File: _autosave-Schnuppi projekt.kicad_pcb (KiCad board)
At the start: 2 copper layers, 23 parts, among them Q1 BC817, Q2 BC817, SW1 SW_Push, SW2 SW_Push, SW3 SW_Push, SW4 SW_Push, SW5 SW_Push, SW6 SW_Push, U13 ESP32-WROOM-32E, U14 DM-OLED096-636, U2 TPS62065DSGR, U5 WE-TVS-82400102, U6 CH340C

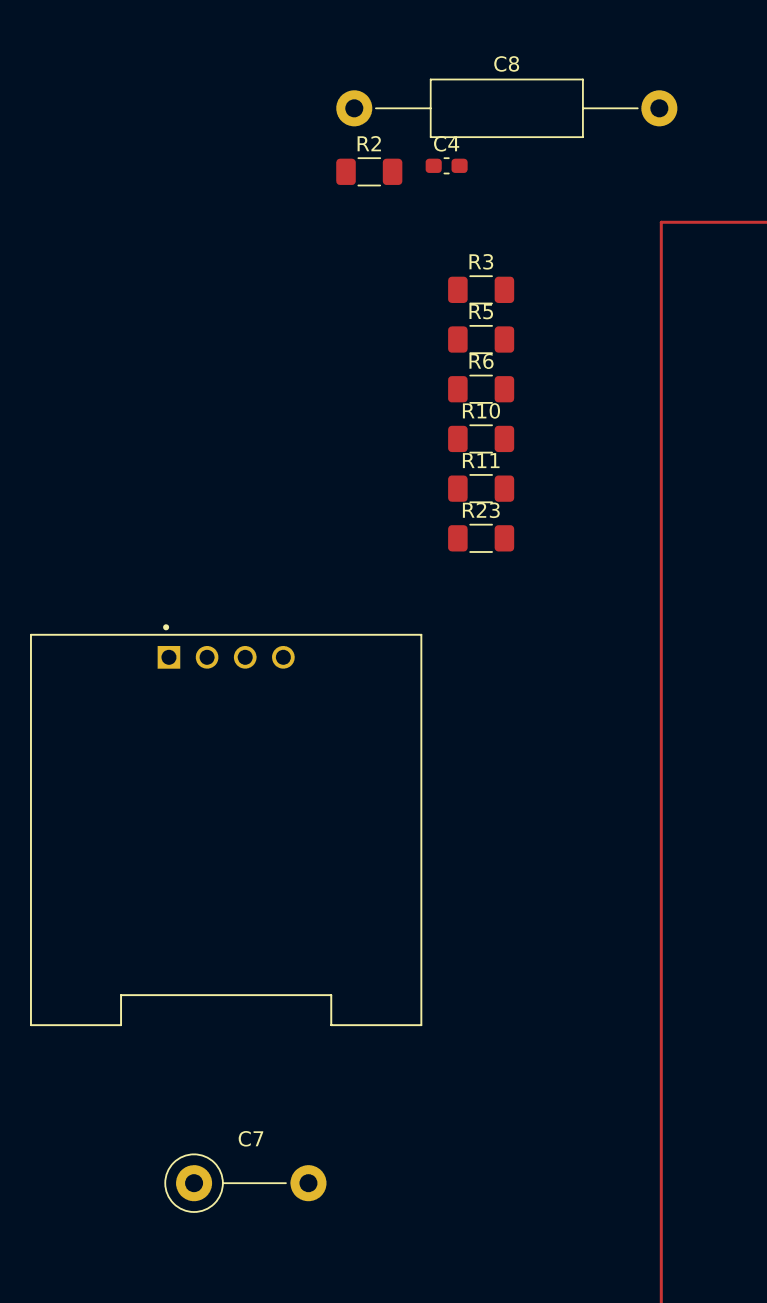
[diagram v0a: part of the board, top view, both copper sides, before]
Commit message: changed resistors
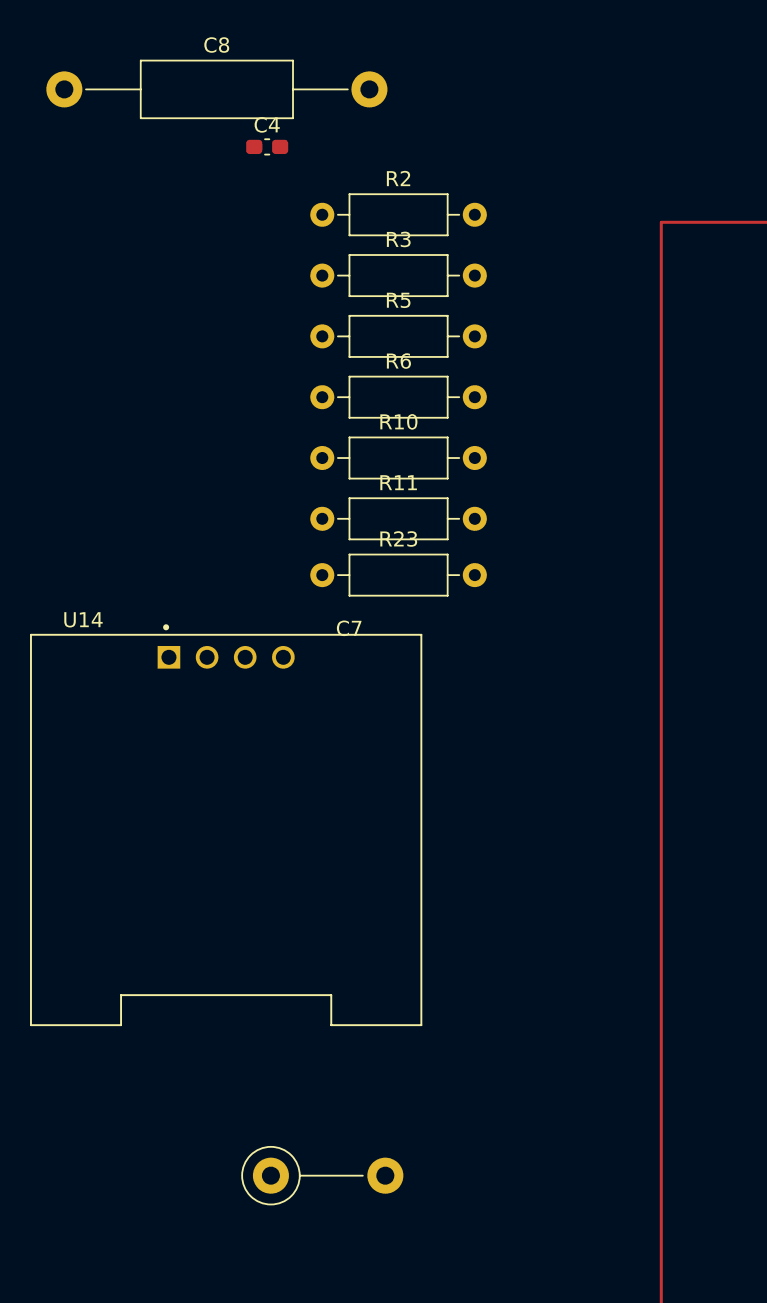
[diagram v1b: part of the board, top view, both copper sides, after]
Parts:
- R10, R11, R2, R23, R3, R5, R6: footprint Resistor_SMD:R_1206_3216Metric_Pad1.30x1.75mm_HandSolder -> Resistor_THT:R_Axial_DIN0207_L6.3mm_D2.5mm_P10.16mm_Horizontal
- moved C8 19.4 mm to (-29.8, 1.15)
- moved C4 12.0 mm to (-16.2, 4.98)
- moved R23 10.9 mm to (-12.6, 33.5)
- moved R11 10.8 mm to (-12.6, 29.8)
- moved R10 10.7 mm to (-12.6, 25.7)
- moved R3 10.6 mm to (-12.6, 13.6)
- moved R6 10.6 mm to (-12.6, 21.6)
- moved R5 10.6 mm to (-12.6, 17.6)
- moved C7 5.14 mm to (-16.0, 73.5)
- moved R2 4.24 mm to (-12.6, 9.50)

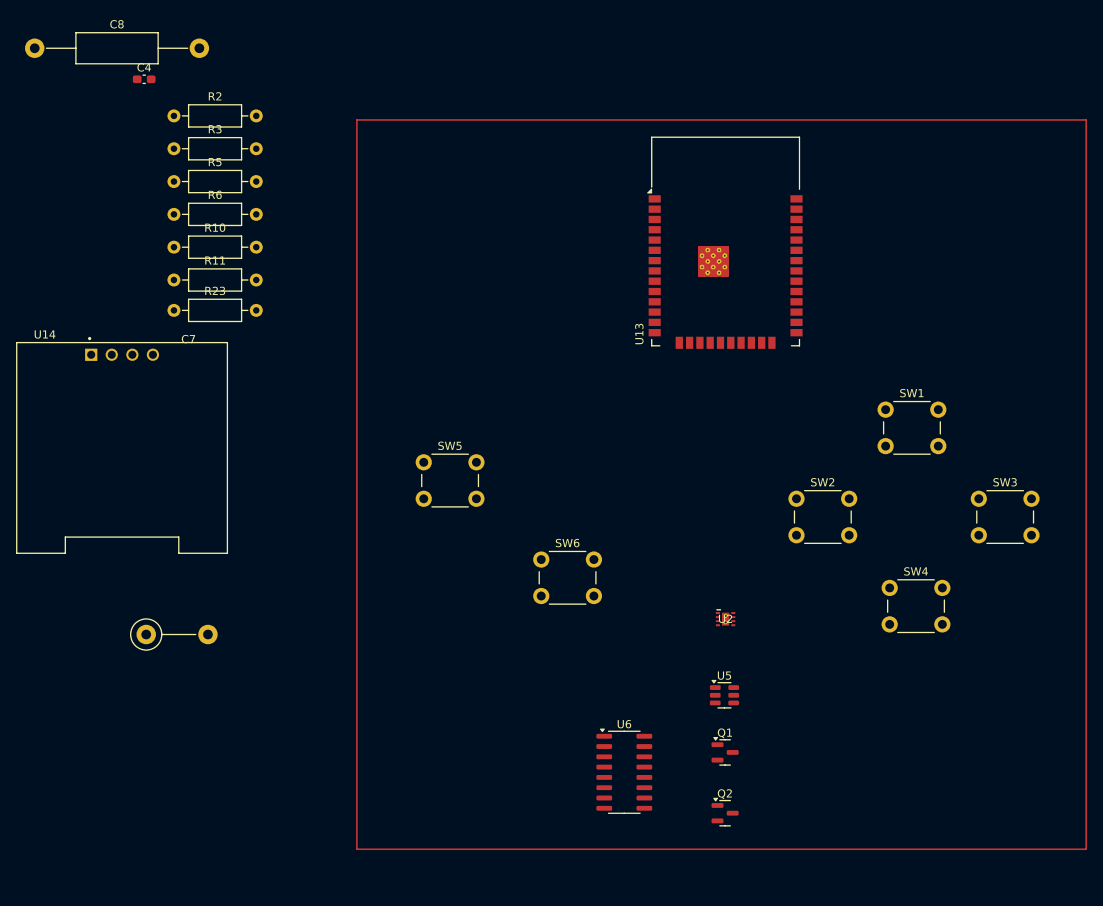
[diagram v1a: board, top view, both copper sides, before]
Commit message: added footprints for resistors
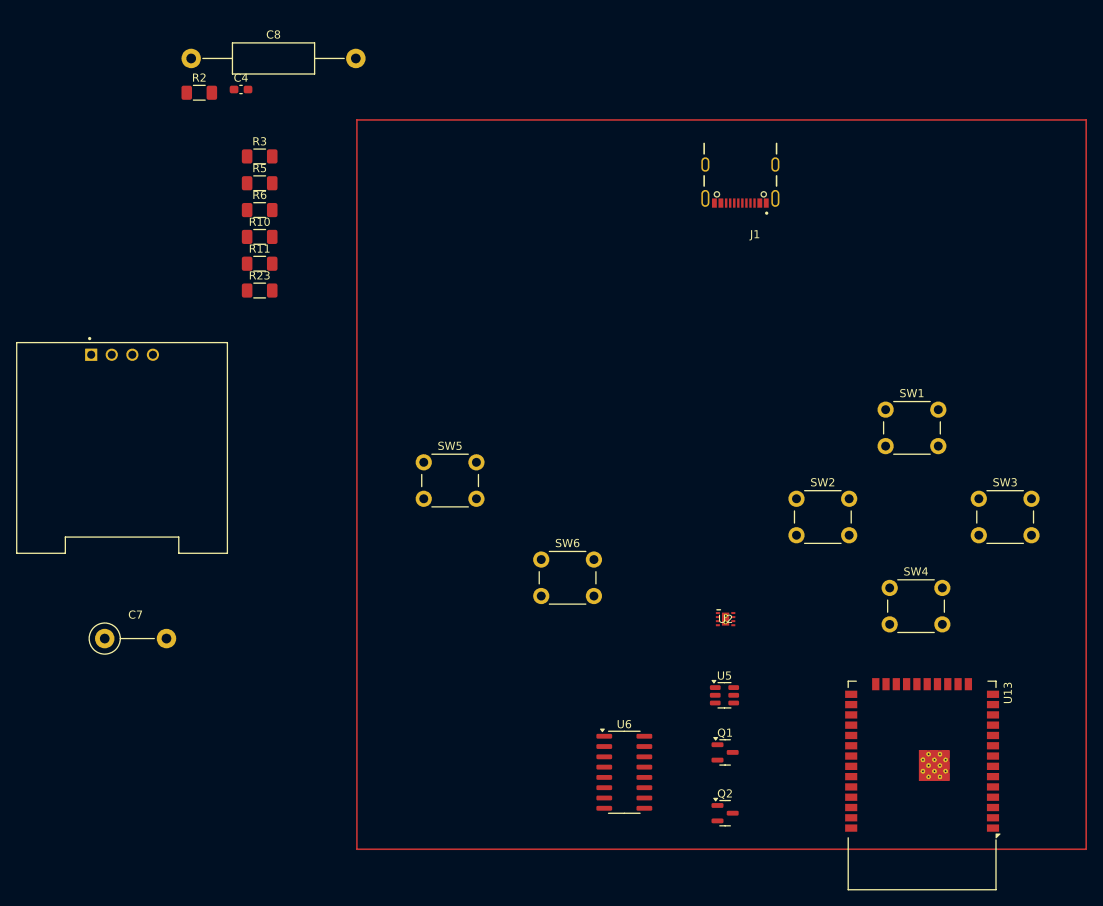
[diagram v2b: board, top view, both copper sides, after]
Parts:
- added J1: USB4105-GF-A, USB4105-GF-A (2):GCT_USB4105-GF-A, F.Cu at (57.3, 15.5)
- R10, R11, R2, R23, R3, R5, R6: footprint Resistor_THT:R_Axial_DIN0207_L6.3mm_D2.5mm_P10.16mm_Horizontal -> Resistor_SMD:R_1206_3216Metric_Pad1.30x1.75mm_HandSolder
- moved U13 65.8 mm to (79.8, 89.1), turned to 180 degrees
- moved C8 19.4 mm to (-10.4, 2.41)
- moved C4 12.0 mm to (-4.30, 6.24)
- moved R23 10.9 mm to (-2.00, 31.1)
- moved R11 10.8 mm to (-2.00, 27.7)
- moved R10 10.7 mm to (-2.00, 24.4)
- moved R3 10.6 mm to (-2.00, 14.5)
- moved R6 10.6 mm to (-2.00, 21.1)
- moved R5 10.6 mm to (-2.00, 17.8)
- moved C7 5.14 mm to (-21.1, 74.0)
- moved R2 4.24 mm to (-9.45, 6.64)
